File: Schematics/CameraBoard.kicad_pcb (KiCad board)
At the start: 4 copper layers, 50 x 100 mm, 73 parts, among them J1 Microsemi_FlashPro-JTAG-10, J2 USB_C_Receptacle, U1 STM32F405RGT6, U2 LDL1117-3.3, U3 TPS22917DBVR, U4 SN65HVD230, U5 TPS22917DBVR, U6 TPS22917DBVR, Y1 8mhz

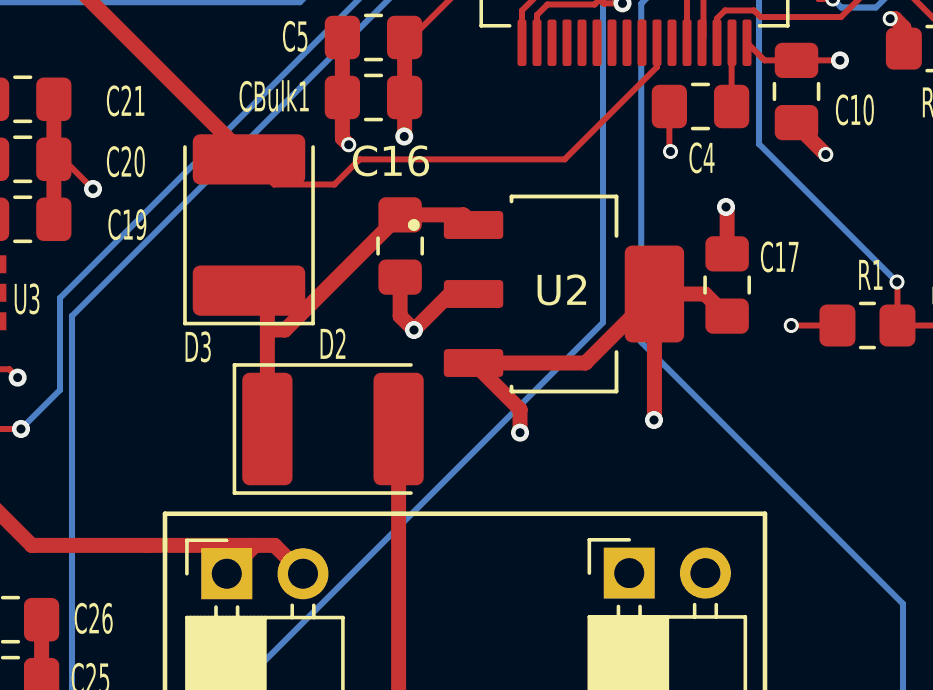
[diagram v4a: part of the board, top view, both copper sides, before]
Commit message: added rules area for ocilator and copper area for ldo
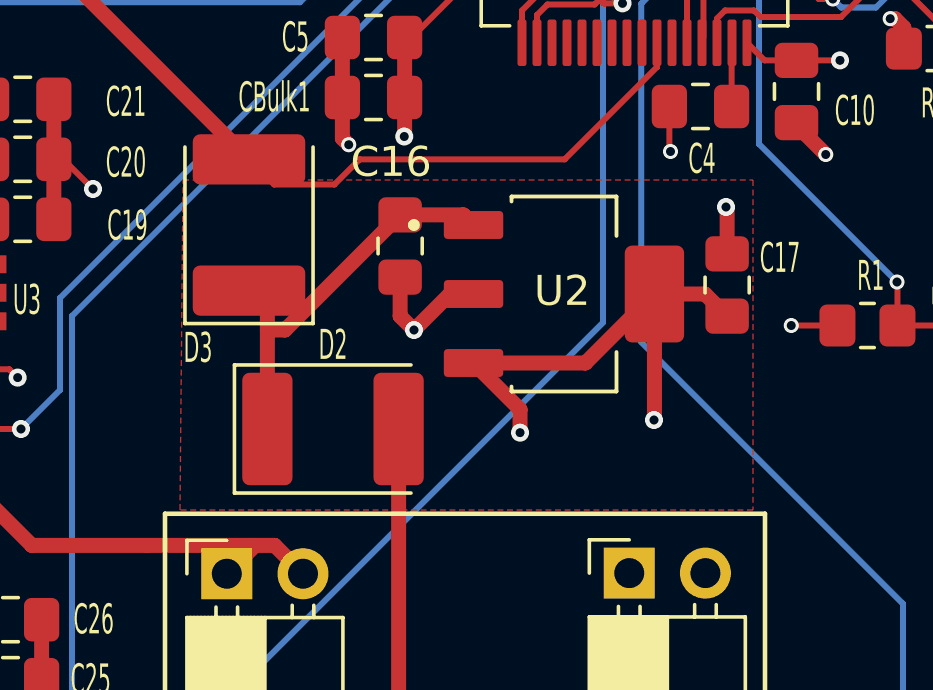
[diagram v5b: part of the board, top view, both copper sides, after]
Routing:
- added copper zone on F.Cu, net (none)
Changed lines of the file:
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@@
 		(net_name "")
 		(layer "F.Cu")
+		(hatch full 0.5)
+		(priority 2)
+		(connect_pads
+			(clearance 0)
+		)
+		(min_thickness 0.25)
+		(filled_areas_thickness no)
+		(fill yes
+			(thermal_gap 0.5)
+			(thermal_bridge_width 0.5)
+			(smoothing fillet)
+			(radius 2)
+			(island_removal_mode 1)
+			(island_area_min 10)
+		)
+		(polygon
+			(pts
+				(xy 85.8 87.9) (xy 104.8 87.9) (xy 104.8 98.9) (xy 85.7 98.9)
+			)
+		)
+	)
+	(zone
+		(net 2)
+		(net_name "GND")
+		(layer "B.Cu")
 		(hatch edge 0.5)
+		(connect_pads
+			(clearance 0.5)
+		)
+		(min_thickness 0.25)
+		(filled_areas_thickness no)
+		(fill yes
+			(thermal_gap 0.5)
+			(thermal_bridge_width 0.5)
+		)
+		(polygon
+			(pts
+				(xy 192.5 32.5) (xy 195.4 155.4) (xy 31.4 157.9) (xy 37.5 32.5)
+			)
+		)
+	)
+	(zone
+		(net 0)
+		(net_name "")
+		(layers "B.Cu" "In2.Cu")
+		(hatch full 0.5)
 		(connect_pads
 			(clearance 0)
@@
 		(polygon
 			(pts
-				(xy 103.8 70.575) (xy 104.15 70.125) (xy 104.15 69.25) (xy 104.25 68.825) (xy 105.35 68.9) (xy 105.875 68.25)
-				(xy 105.875 67) (xy 105.525 66.675) (xy 105.85 66.125) (xy 105.85 63.95) (xy 106.3 63.425) (xy 105.85 62.825)
-				(xy 105.875 62.475) (xy 105.25 61.85) (xy 104.975 61.225) (xy 101.375 61.225) (xy 100.75 61.575)
-				(xy 99.475 61.575) (xy 99.125 62.7) (xy 98.05 64.1) (xy 97.25 65.1) (xy 97.6 66.925) (xy 97.925 68.9)
-				(xy 99.625 70.35) (xy 100.225 70.75) (xy 100.3 70.575) (xy 99.975 70.35) (xy 98.15 68.825) (xy 97.85 68.05)
-				(xy 97.675 66.55) (xy 97.425 65.2) (xy 98.1 64.3) (xy 99.2 62.85) (xy 99.525 61.775) (xy 100.775 61.75)
-				(xy 101.4 61.325) (xy 104.825 61.375) (xy 104.975 61.5) (xy 105.175 61.825) (xy 105.8 62.55) (xy 105.8 63.025)
-				(xy 106.2 63.4) (xy 105.95 63.8) (xy 105.75 64.05) (xy 105.75 66.1) (xy 105.425 66.675) (xy 105.775 67.175)
-				(xy 105.7 68.2) (xy 105.375 68.7) (xy 105.25 68.85) (xy 104.225 68.775) (xy 104.025 69.45) (xy 104.05 70.125)
-				(xy 103.675 70.525)
+				(xy 97.546362 67.970197) (xy 97.646362 64.870197) (xy 99.246362 63.570197) (xy 99.446362 61.7) (xy 100.746362 61.870197)
+				(xy 100.846362 61.370197) (xy 104.946362 61.470197) (xy 106.146362 62.970197) (xy 105.546362 66.270197)
+				(xy 105.146362 66.670197) (xy 105.546362 66.970197) (xy 105.546362 68.070197) (xy 104.746362 68.670197)
+				(xy 104.146362 68.870197) (xy 103.946362 70.070197) (xy 103.646362 70.270197) (xy 103.446362 70.570197)
+				(xy 101.246362 70.570197) (xy 99.946362 70.570197)
 			)
 		)
-	)
-	(zone
-		(net 2)
-		(net_name "GND")
-		(layer "B.Cu")
-		(hatch edge 0.5)
-		(connect_pads
-			(clearance 0.5)
-		)
-		(min_thickness 0.25)
-		(filled_areas_thickness no)
-		(fill yes
-			(thermal_gap 0.5)
-			(thermal_bridge_width 0.5)
-		)
-		(polygon
-			(pts
-				(xy 192.5 32.5) (xy 195.4 155.4) (xy 31.4 157.9) (xy 37.5 32.5)
-			)
-		)

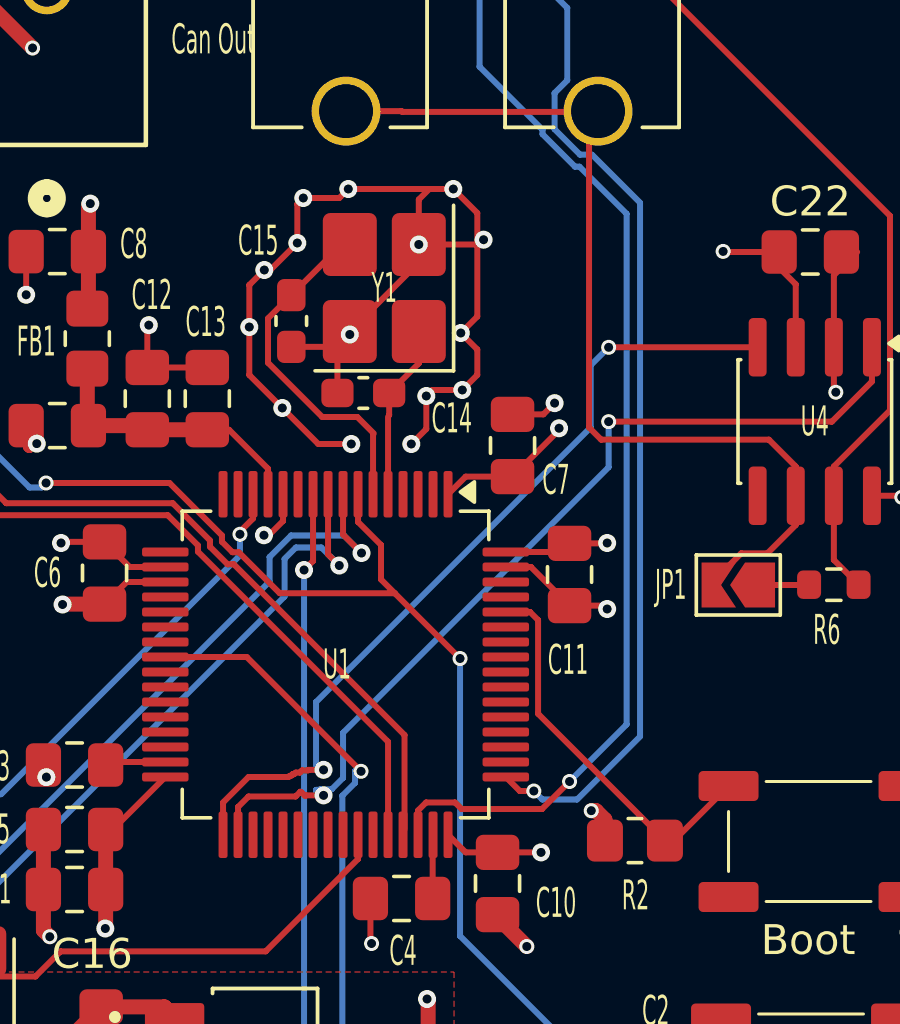
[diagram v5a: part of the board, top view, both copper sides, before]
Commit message: fixed ocilator route lengths
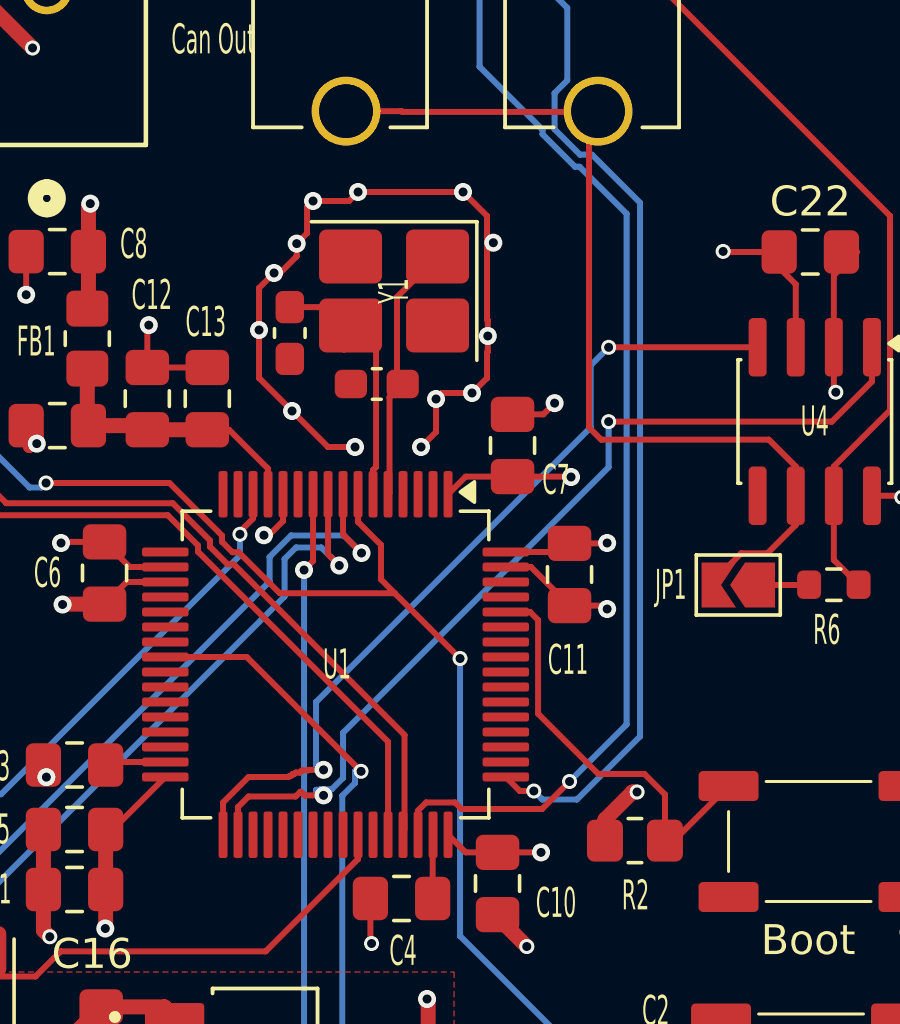
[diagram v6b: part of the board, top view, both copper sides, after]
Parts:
- moved C14 0.54 mm to (102.2, 68.3)
- moved C15 0.40 mm to (99.3, 66.6)
- moved Y1 0.34 mm to (102.8, 65.2), turned to 180 degrees
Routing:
- net GND: track 119.5 -> 107.7 mm, vias 42 -> 40
- net /MCU/OSC IN: track 5.79 -> 9.36 mm
- net /MCU/OSC OUT: track 11.7 -> 9.71 mm
- net /MCU/BOOT0: track 13.2 -> 14.1 mm

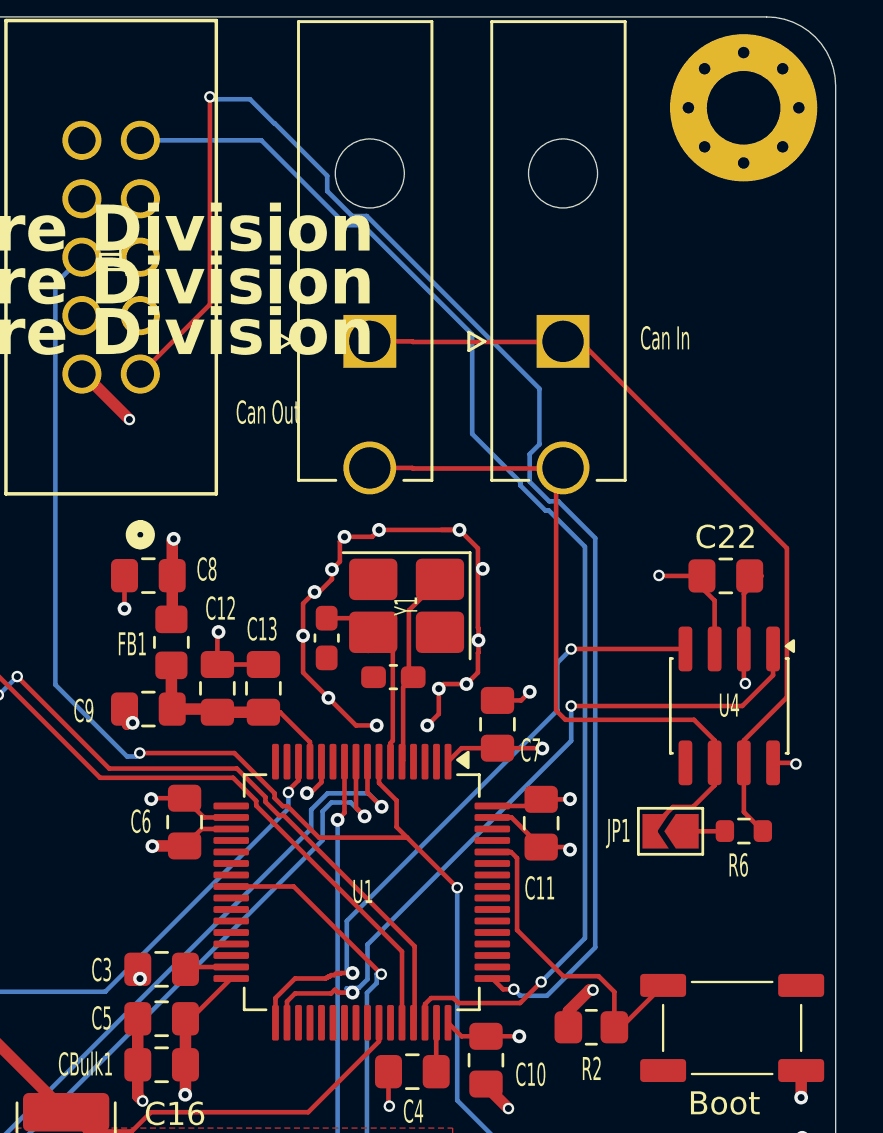
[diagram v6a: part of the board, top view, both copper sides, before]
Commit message: fixed rule area and cap
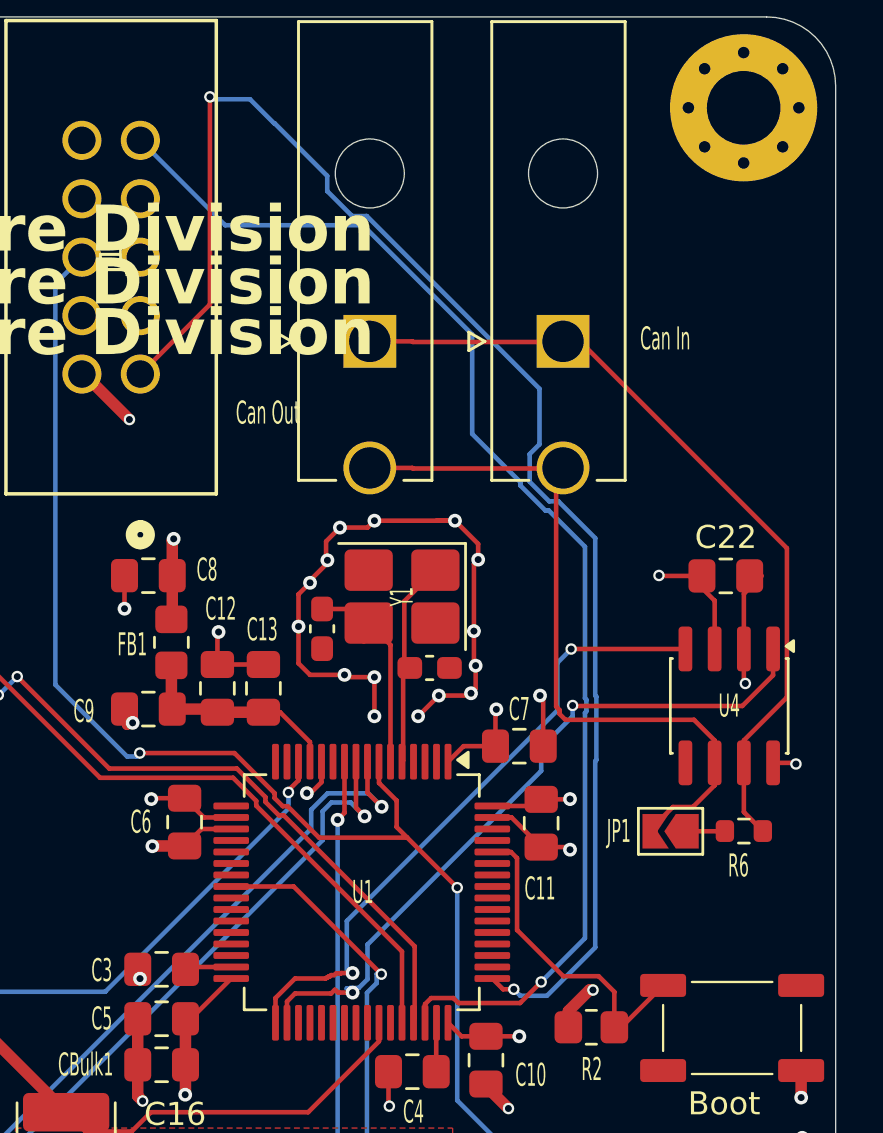
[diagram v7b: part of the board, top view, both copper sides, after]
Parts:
- moved C14 1.63 mm to (103.8, 67.9), turned to 0 degrees
- moved C7 1.34 mm to (107.7, 71.3), turned to 0 degrees
- moved C15 0.45 mm to (99.1, 66.2)
- moved Y1 0.45 mm to (102.6, 64.8)
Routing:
- net GND: track 107.7 -> 109.9 mm, vias 40 -> 42
